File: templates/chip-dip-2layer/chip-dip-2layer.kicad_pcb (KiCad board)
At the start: 2 copper layers, 40.6 x 55.2 mm, 2 parts, among them J13 DIP-HEADER-2x20, J14 DIP-HEADER-2x20

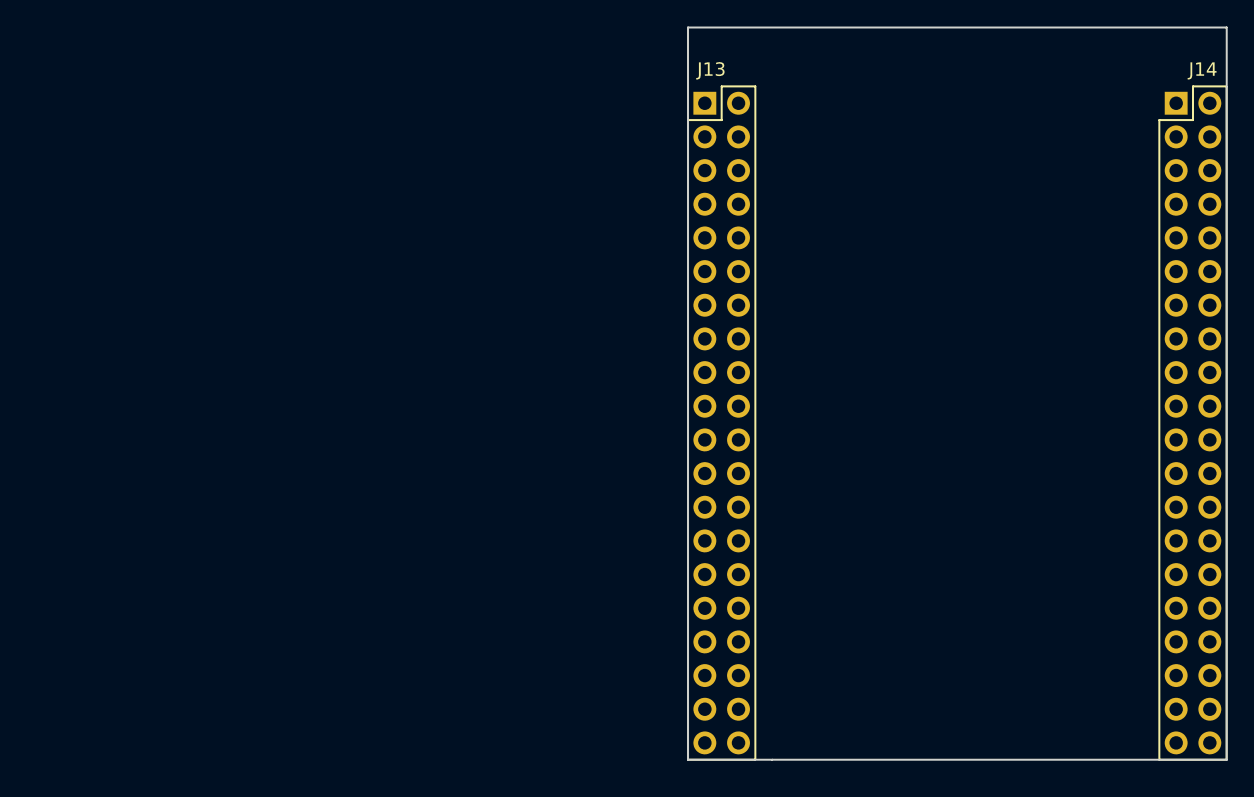
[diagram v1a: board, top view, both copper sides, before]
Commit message: Add fab notes to Dwgs.User
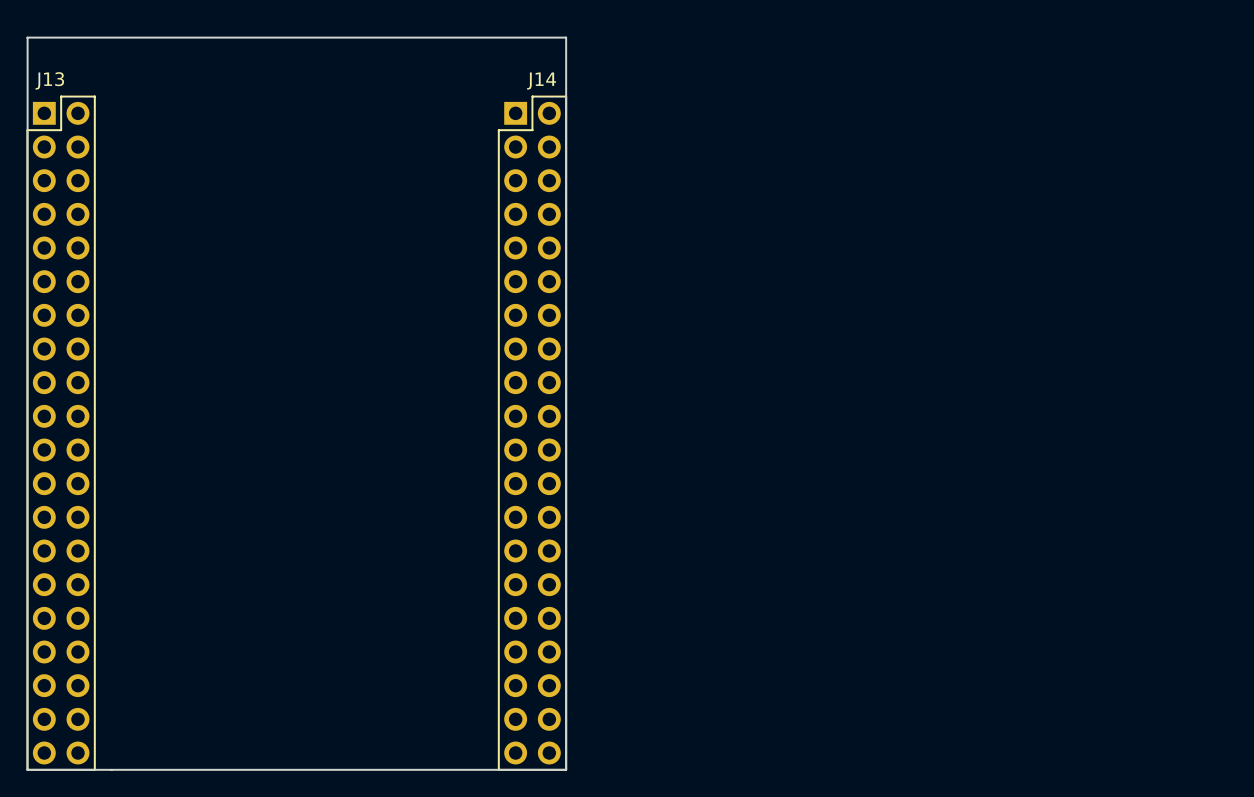
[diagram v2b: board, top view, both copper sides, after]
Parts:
- moved J14 49.8 mm to (61.9, 51.6)
- moved J13 49.8 mm to (26.4, 51.6)
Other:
- outline, holes or cut-outs redrawn
- board text added: "FABRICATION NOTES 1. THIS IS A 2 LAYER BOARD. 2. EXTERNAL LAYERS SHALL HAVE 1 OZ COPPER. 3. MATERIAL: FR4 AND 0.062 INCH +/- 10% THICK. 4. BOARDS SHALL BE ROHS COMPLIANT. 5. MANUFACTURE IN ACCORDANCE WITH IPC-6012 CLASS 2 6. MASK: BOTH SIDES OF THE BOARD SHALL HAVE SOLDER MASK (ANY COLOR) OVER BARE COPPER. 7. SILK: BOTH SIDES OF THE BOARD SHALL HAVE WHITE SILKSCREEN. DO NOT PLACE SILK OVER BARE C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"
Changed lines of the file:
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@@
-(kicad_pcb (version 4) (host pcbnew 4.0.5-e0-6337~49~ubuntu16.04.1)
+(kicad_pcb (version 4) (host pcbnew 4.0.7-e2-6376~58~ubuntu16.04.1)
   (general
     (links 10)
     (no_connects 10)
-    (area 74.854999 45.009999 115.645001 100.405001)
+    (area 72.123 45.009999 116.339001 101.129001)
     (thickness 1.6)
-    (drawings 5)
+    (drawings 6)
     (tracks 0)
     (zones 0)
@@
   )
   (module CHIP-DIPs:DIP_Header_2x20 locked (layer F.Cu)
-    (at 76.2 50.8)
+    (at 26.3652 51.562)
     (descr "Standard 2x20 DIP header based on KiCad Pin Header 2x20")
     (tags "pin header")
@@
   )
   (module CHIP-DIPs:DIP_Header_2x20 locked (layer F.Cu)
-    (at 111.76 50.8)
+    (at 61.9252 51.562)
     (descr "Standard 2x20 DIP header based on KiCad Pin Header 2x20")
     (tags "pin header")
@@
     )
   )
-  (gr_line (start 74.93 45.085) (end 115.57 45.085) (layer Edge.Cuts) (width 0.15))
-  (gr_line (start 115.57 45.085) (end 115.57 100.33) (layer Edge.Cuts) (width 0.15))
-  (gr_line (start 81.28 100.33) (end 115.57 100.33) (layer Edge.Cuts) (width 0.15))
-  (gr_line (start 74.93 100.33) (end 81.28 100.33) (layer Edge.Cuts) (width 0.15))
-  (gr_line (start 74.93 45.085) (end 74.93 100.33) (layer Edge.Cuts) (width 0.15))
+  (gr_text "FABRICATION NOTES\n\n1. THIS IS A 2 LAYER BOARD. \n2. EXTERNAL LAYERS SHALL HAVE 1 OZ COPPER.\n3. MATERIAL: FR4 AND 0.062 INCH +/- 10% THICK.\n4. BOARDS SHALL BE ROHS COMPLIANT. \n5. MANUFACTURE IN ACCORDANCE WITH IPC-6012 CLASS 2\n6. MASK: BOTH SIDES OF THE BOARD SHALL HAVE \n   SOLDER MASK (ANY COLOR) OVER BARE COPPER. \n7. SILK: BOTH SIDES OF THE BOARD SHALL HAVE \n   WHITE SILKSCREEN. DO NOT PLACE SILK OVER BARE COPPER.\n8. FINISH: ENIG.\n9. MINIMUM TRACE WIDTH - 0.006 INCH.\n   MINIMUM SPACE - 0.006 INCH.\n   MINIMUM HOLE DIA - 0.013 INCH. \n10. MAX HOLE PLACEMENT TOLERANCE OF +/- 0.003 INCH.\n11. MAX HOLE DIAMETER TOLERANCE OF +/- 0.003 INCH AFTER PLATING." (at 108.3564 77.2668) (layer Dwgs.User)
+    (effects (font (size 2.54 2.54) (thickness 0.254)) (justify left))
+  )
+  (gr_line (start 25.0952 45.847) (end 65.7352 45.847) (layer Edge.Cuts) (width 0.15))
+  (gr_line (start 65.7352 45.847) (end 65.7352 101.092) (layer Edge.Cuts) (width 0.15))
+  (gr_line (start 31.4452 101.092) (end 65.7352 101.092) (layer Edge.Cuts) (width 0.15))
+  (gr_line (start 25.0952 101.092) (end 31.4452 101.092) (layer Edge.Cuts) (width 0.15))
+  (gr_line (start 25.0952 45.847) (end 25.0952 101.092) (layer Edge.Cuts) (width 0.15))
 )
